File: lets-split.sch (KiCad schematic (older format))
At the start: 56 parts, among them J1 USB_C_Receptacle_USB2.0, SW1 Key_Tab, SW10 Key_D, SW11 Key_F, SW12 Key_G, SW13 Key_Shift, SW14 Key_Z, SW15 Key_X, SW16 Key_C, SW17 Key_V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

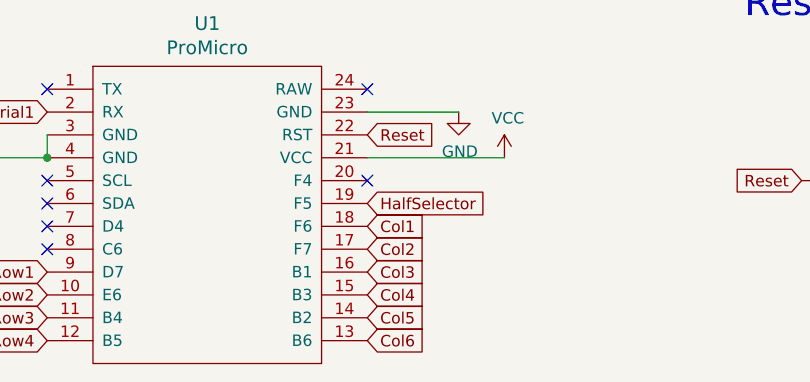
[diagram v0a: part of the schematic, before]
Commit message: Reversed column pin order to tidy PCB
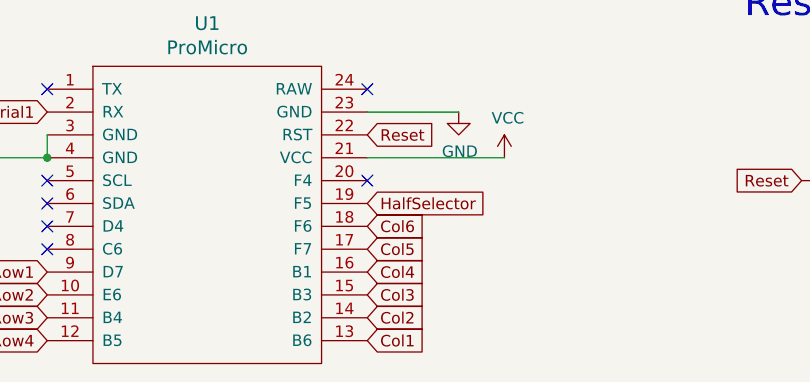
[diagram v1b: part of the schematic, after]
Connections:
- net Col1: now also U1.13 (B6); no longer U1.18 (F6)
- net Col2: now also U1.14 (B2); no longer U1.17 (F7)
- net Col3: now also U1.15 (B3); no longer U1.16 (B1)
- net Col4: now also U1.16 (B1); no longer U1.15 (B3)
- net Col5: now also U1.17 (F7); no longer U1.14 (B2)
- net Col6: now also U1.18 (F6); no longer U1.13 (B6)
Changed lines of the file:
@@
 Text GLabel 2150 6950 0    50   Input ~ 0
 Row4
+Text GLabel 3550 6450 2    50   Input ~ 0
+Col6
+Text GLabel 3550 6550 2    50   Input ~ 0
+Col5
+Text GLabel 3550 6650 2    50   Input ~ 0
+Col4
+Text GLabel 3550 6750 2    50   Input ~ 0
+Col3
+Text GLabel 3550 6850 2    50   Input ~ 0
+Col2
 Text GLabel 3550 6950 2    50   Input ~ 0
-Col6
-Text GLabel 3550 6850 2    50   Input ~ 0
-Col5
-Text GLabel 3550 6750 2    50   Input ~ 0
-Col4
-Text GLabel 3550 6650 2    50   Input ~ 0
-Col3
-Text GLabel 3550 6550 2    50   Input ~ 0
-Col2
-Text GLabel 3550 6450 2    50   Input ~ 0
 Col1
 $Comp
